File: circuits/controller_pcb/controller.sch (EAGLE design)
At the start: 26 parts, among them J1 USB-MICROB, Q1 BSS138, Q2 FDN340P, U1 ATMEGA328P_TQFP, Y2 12MHz

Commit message: Merged multiple board into a single one - controller - UNTESTED
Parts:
- removed J1: USB-MICROB, SparkFun-Connectors:USB-MICROB
- removed Q1: BSS138, SparkFun-DiscreteSemi:MOSFET-NCHANNELBSS138
- removed R1: 10k, rcl:R-EU_R0402
- removed Y2: 12MHz, crystals_golledge_full_v1-0:GSX-531
- added C11, C12, C13, C14, C15, C8: 100n, rcl:C-EUC0402K
- added IC1: DS1820, DS1820:DS1820
- added J3: USB-MICROB", SparkFun-Connectors:USB-MICROB"
- added Q3: SI2333DS, transistor-fet:SI2333DS
- added Q5: BSS138, transistor-fet:BSS138
- added R10, R11: (no value), rcl:R-EU_R0402
- added R4, R8: 10k, rcl:R-EU_R0402
- added R5: 1k, rcl:R-EU_R0402
- added R6, R7: 4k7, rcl:R-EU_R0402
- added R9: 0.1, rcl:R-EU_R2512
- added TP1, TP2, TP3, TP5, TP6, TP7: TPTP07SQ, testpad:TPTP07SQ
- added U$7: 1X6, headers(.05in):1X6
- added U$8: INA219AIDCNR, INA219AIDCNR:INA219AIDCNR
- added U$9: 12MHz, crystals_golledge_full_v1-0:GSX-331
- added U2: MIC5219 5V, SparkFun-PowerIC:V_REG_MIC52195V
- C1: value 22p -> 47u; device rcl:C-EUC0402K -> rcl:C-EUC1206
- C2: value 22p -> 10u; device rcl:C-EUC0402K -> rcl:C-EUC0603K
- C3: value 22p -> 100n
- C6, C7, C9: value 100n -> 22p
- R2, R3: value (none) -> 10k
- U$1: value 1X3 -> DRV8835DSSR; device headers(.05in):1X3 -> DRV8835:DRV8835DSSR
- U$2: value 1X3 -> CH340G; device headers(.05in):1X3 -> ch340g:CH340G
- U$3, U$4: value 1X8MALE -> 504050; device headers(.05in):1X8MALE -> con-molex-picolock:504050
- U$5: value CH340G -> MG996R_MOTOR; device ch340g:CH340G -> MG996R-Motor:MG996R_MOTOR
- U$6: value 16Mhz -> 16MHz
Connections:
- net N$13 renamed LED_R_
- net N$14 renamed LED_G_
- removed net CS: U1.PB2(SS/OC1B)
- removed net DATA_DIR_BIT: Q1.G, U1.PD2(INT0)
- removed net DI: U1.PD6(AIN0)
- removed net DIR: U1.PB0(ICP)
- removed net DS18B20: U1.PD5(T1)
- removed net EN: U1.PD7(AIN1)
- removed net N$15: LED1.B, RN1B.2
- removed net N$6: F1.1, J1.VBUS
- removed net N$7: Q1.S, U1.PD1(TXD)
- removed net PWM_1: U$2.3, U1.ADC7
- removed net SCK: U1.PB5(SCK)
- removed net SI: U1.PB3(MOSI/OC2)
- removed net SO: U1.PB4(MISO)
- new net 1WIRE: IC1.DQ, R7.2, U1.PD4(XCK/T0)
- new net IN1/PHASE: U$1.AIN1/APHASE, U$1.BIN1/BPHASE, U1.PB1(OC1A)
- new net IN2/ENBL: U$1.AIN2/AENBL, U$1.BIN2/BENBL, U1.PB2(SS/OC1B)
- new net LED_B: RN1A.1, U1.PC1(ADC1)
- new net LED_B_: LED1.B, RN1A.2
- new net LED_G: RN1C.1, U1.PC0(ADC0)
- new net LED_R: RN1D.1, U1.ADC7
- new net MODE: U$1.MODE, U1.PB0(ICP)
- new net MOT+: U$1.AOUT1, U$1.BOUT1, U$5.MOT-
- new net MOT-: U$1.AOUT2, U$1.BOUT2, U$5.MOT+
- new net N$12: C13.1, U2.BP
- new net N$14: TP1.TP, U1.PB5(SCK)
- new net VCC: Q3.D, R8.2, U$3.2, U$4.2
- new net VDD: C15.1, R9.1, U$1.VM, U$8.IN-
- new net VIN_ADC: R10.1, R11.2, U1.PC3(ADC3)
- net 5V: now also C14.1, C2.1, C4.1, IC1.VDD, R2.2, R3.2, R4.2, R6.1, R7.1, TP6.TP, U$1.VCC, U$7.3, U$8.VS, U2.OUT; no longer C7.1, C9.1, R1.2, U$2.1, U$5.VCC
- net D+: now also J3.D+, U$2.D+; no longer J1.D+, U$5.D+
- net D-: now also J3.D-, U$2.D-; no longer J1.D-, U$5.D-
- net DATA: now also Q5.D, R5.2, R6.2, U$3.3, U$4.3; no longer Q1.D, U1.PD0(RXD)
- net GND: now also C11.2, C12.2, C13.2, C14.2, C15.2, C8.2, IC1.GND, J3.GND, J3.SHIELD, Q3.G, Q5.S, R11.1, R8.1, TP7.TP, U$1.GND, U$1.PGND, U$2.GND, U$3.1, U$4.1, U$6.2, U$6.4, U$7.5, U$8.A0, U$8.A1, U$8.GND, U$9.2, U$9.4, U2.GND; no longer C3.2, J1.GND, R2.1, U$1.2, U$5.GND
- net INT: now also U$7.1, U1.PD2(INT0); no longer U$2.2, U1.ADC6
- net N$1: now also C6.1, U$6.1, U1.PB7(XTAL2/TOSC2); no longer C2.1, U$5.XO, Y2.1
- net N$10: now also C11.1, F1.1, J3.VBUS, U$2.VCC; no longer RN1C.1, U1.PC2(ADC2)
- net N$11: now also C8.1, U$2.V3; no longer RN1D.1, U1.PC1(ADC1)
- net N$2: now also C7.1, U$6.3, U1.PB6(XTAL1/TOSC1); no longer C3.1, U$5.XI, Y2.3
- net N$3: now also TP3.TP, U1.PB3(MOSI/OC2); no longer C1.1, U$6.3, U1.PB7(XTAL2/TOSC2)
- net N$4: now also TP2.TP, U1.PB4(MISO); no longer C4.1, U$5.V3
- net N$5: now also C3.1, U$2.DTR; no longer C10.1, U$6.1, U1.PB6(XTAL1/TOSC1)
- net N$8: now also C10.1, U$2.XI, U$9.3; no longer R2.2, R3.1, U1.PC0(ADC0)
- net N$9: now also C9.1, U$2.XO, U$9.1; no longer RN1B.1, U1.PC3(ADC3)
- net PWM: now also U$7.2, U1.PD3(INT1); no longer U1.PB1(OC1A)
- net RST: now also C3.2, R4.1, TP5.TP; no longer C6.1, R1.1
- net RX: now also R5.1, U$2.TX, U1.PD0(RXD); no longer U$5.RX, U1.PD3(INT1)
- net SCL: now also R3.1, U$7.6, U$8.SCL; no longer U$1.1
- net SDA: now also R2.1, U$7.4, U$8.SDA; no longer U$1.3
- net TX: now also Q5.G, U$2.RX, U1.PD1(TXD); no longer U$5.TX, U1.PD4(XCK/T0)
- net VIN: now also C1.1, C12.1, Q3.S, R10.2, R9.2, U$8.IN+, U2.EN, U2.IN; no longer R3.2
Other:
- note removed: "+5V selector (USB)"
- note removed: "ADD reset to breakout pins"
- moved on the sheet: C1, C10, C2, C3, C4, C5, C6, C7, C9, F1, LED1, Q2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

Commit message: Updated controller circuit - UNTESTED
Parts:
- removed U$7: 1X6, headers(.05in):1X6
- added D1: IN5819, SparkFun-DiscreteSemi:MBRA140
- added MISO, SCK: TPTP07SQ, testpad:TPTP07SQ
- added RN2: (no value), resistor-dil:4R-NYC124
- added U$10: 1X5, headers(.05in):1X5
- R5: value 1k -> 10k
- TP1, TP2: value TPTP07SQ -> PTR1TP12R; device testpad:TPTP07SQ -> testpad:PTR1TP12R
- renumbered TP3 to MOSI, TP5 to RST, TP6 to 5V, TP7 to GND
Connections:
- removed net PWM: U$7.2, U1.PD3(INT1)
- new net HD_DIR: Q5.G, R5.2, U1.PD3(INT1)
- new net N$13: TP2.TP, U1.PD5(T1)
- new net N$15: RN2A.2, U$2.RX
- new net N$6: RN2D.2, U$2.TX
- new net N$7: TP1.TP, U$3.4, U$4.4
- net 5V: now also U$10.2, U$2.VCC; no longer U$7.3
- net DATA: now also D1.A, Q5.S; no longer Q5.D, R5.2
- net GND: now also R5.1, U$10.4; no longer Q5.S, U$7.5
- net INT: now also U$10.1; no longer U$7.1
- net N$10: no longer U$2.VCC
- net N$14: now also SCK.TP; no longer TP1.TP
- net N$4: now also MISO.TP; no longer TP2.TP
- net RX: now also Q5.D, RN2D.1; no longer R5.1, U$2.TX
- net SCL: now also U$10.5; no longer U$7.6
- net SDA: now also U$10.3; no longer U$7.4
- net TX: now also D1.C, RN2A.1; no longer Q5.G, U$2.RX
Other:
- moved on the sheet: C10, C11, C14, C15, C3, C8, C9, F1, J3, Q2, Q5, R10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

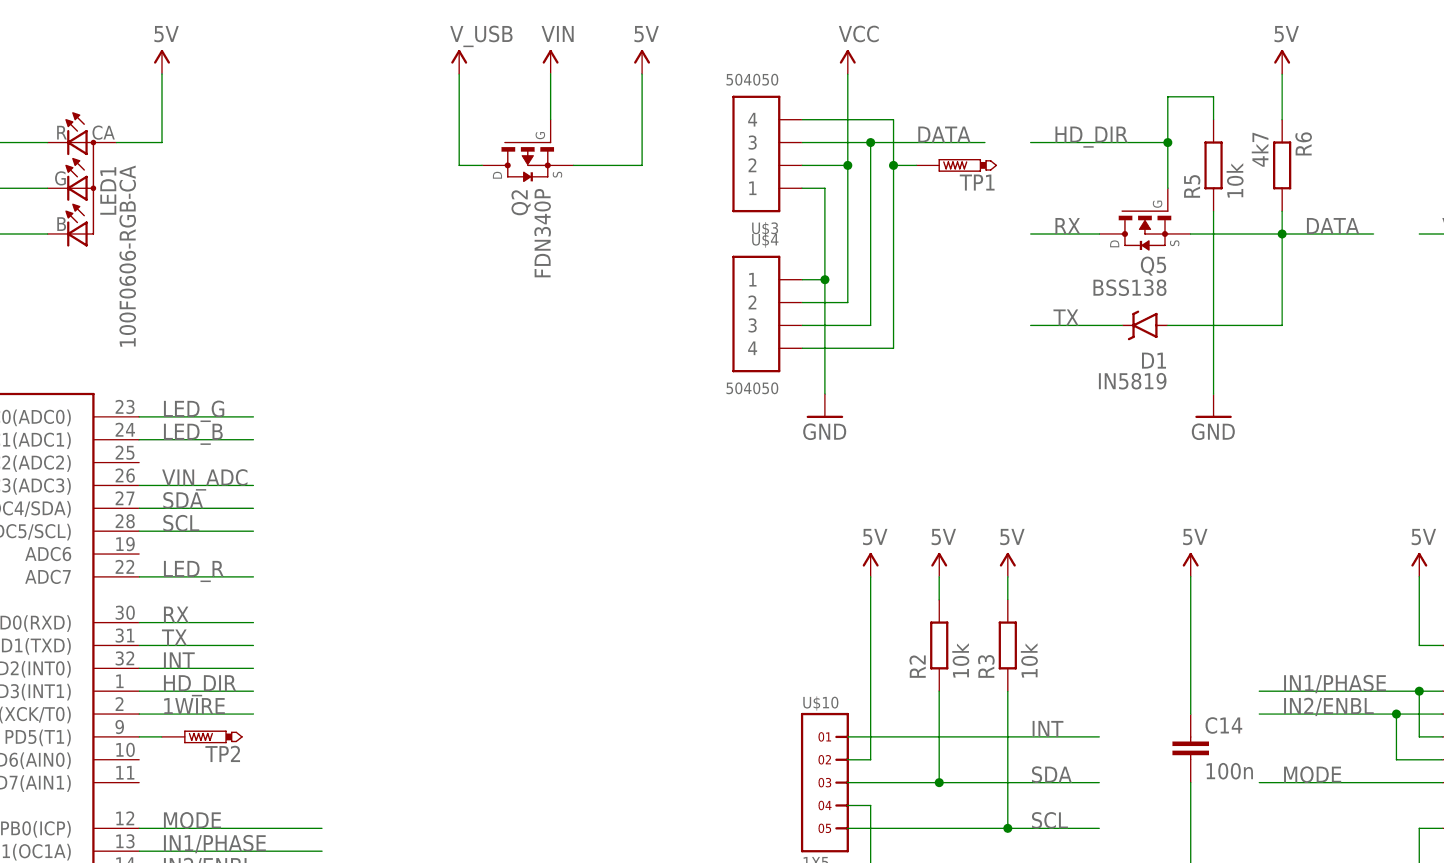
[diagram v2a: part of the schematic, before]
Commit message: Corrected Q5 orientation - UNTESTED
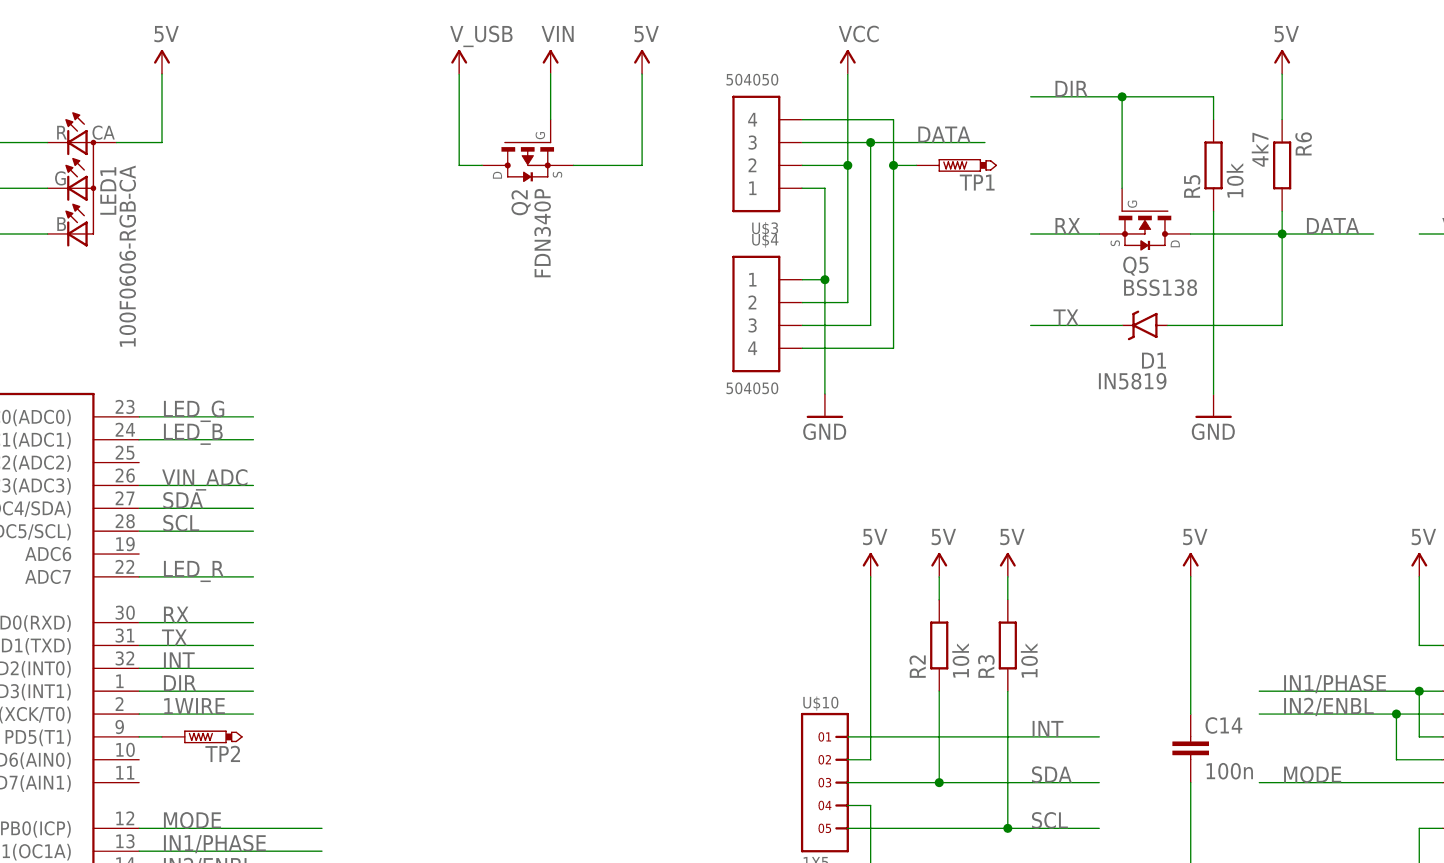
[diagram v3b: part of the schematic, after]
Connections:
- net HD_DIR renamed DIR
- net DATA: now also Q5.D; no longer Q5.S
- net RX: now also Q5.S; no longer Q5.D
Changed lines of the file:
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@@
 <grid distance="0.1" unitdist="inch" unit="inch" style="lines" multiple="1" display="no" altdistance="0.01" altunitdist="inch" altunit="inch"/>
 <layers>
-<layer number="1" name="Top" color="4" fill="1" visible="yes" active="no"/>
-<layer number="16" name="Bottom" color="1" fill="1" visible="yes" active="no"/>
-<layer number="17" name="Pads" color="2" fill="1" visible="yes" active="no"/>
-<layer number="18" name="Vias" color="2" fill="1" visible="yes" active="no"/>
-<layer number="19" name="Unrouted" color="6" fill="1" visible="yes" active="no"/>
-<layer number="20" name="Dimension" color="15" fill="1" visible="yes" active="no"/>
-<layer number="21" name="tPlace" color="7" fill="1" visible="yes" active="no"/>
-<layer number="22" name="bPlace" color="7" fill="1" visible="yes" active="no"/>
-<layer number="23" name="tOrigins" color="15" fill="1" visible="yes" active="no"/>
-<layer number="24" name="bOrigins" color="15" fill="1" visible="yes" active="no"/>
-<layer number="25" name="tNames" color="7" fill="1" visible="yes" active="no"/>
-<layer number="26" name="bNames" color="7" fill="1" visible="yes" active="no"/>
-<layer number="27" name="tValues" color="7" fill="1" visible="yes" active="no"/>
-<layer number="28" name="bValues" color="7" fill="1" visible="yes" active="no"/>
+<layer number="1" name="Top" color="4" fill="1" visible="no" active="no"/>
+<layer number="16" name="Bottom" color="1" fill="1" visible="no" active="no"/>
+<layer number="17" name="Pads" color="2" fill="1" visible="no" active="no"/>
+<layer number="18" name="Vias" color="2" fill="1" visible="no" active="no"/>
+<layer number="19" name="Unrouted" color="6" fill="1" visible="no" active="no"/>
+<layer number="20" name="Dimension" color="15" fill="1" visible="no" active="no"/>
+<layer number="21" name="tPlace" color="7" fill="1" visible="no" active="no"/>
+<layer number="22" name="bPlace" color="7" fill="1" visible="no" active="no"/>
+<layer number="23" name="tOrigins" color="15" fill="1" visible="no" active="no"/>
+<layer number="24" name="bOrigins" color="15" fill="1" visible="no" active="no"/>
+<layer number="25" name="tNames" color="7" fill="1" visible="no" active="no"/>
+<layer number="26" name="bNames" color="7" fill="1" visible="no" active="no"/>
+<layer number="27" name="tValues" color="7" fill="1" visible="no" active="no"/>
+<layer number="28" name="bValues" color="7" fill="1" visible="no" active="no"/>
 <layer number="29" name="tStop" color="7" fill="3" visible="no" active="no"/>
 <layer number="30" name="bStop" color="7" fill="6" visible="no" active="no"/>
@@
 <layer number="35" name="tGlue" color="7" fill="4" visible="no" active="no"/>
 <layer number="36" name="bGlue" color="7" fill="5" visible="no" active="no"/>
-<layer number="37" name="tTest" color="7" fill="1" visible="yes" active="no"/>
-<layer number="38" name="bTest" color="7" fill="1" visible="yes" active="no"/>
+<layer number="37" name="tTest" color="7" fill="1" visible="no" active="no"/>
+<layer number="38" name="bTest" color="7" fill="1" visible="no" active="no"/>
 <layer number="39" name="tKeepout" color="4" fill="11" visible="no" active="no"/>
 <layer number="40" name="bKeepout" color="1" fill="11" visible="no" active="no"/>
@@
 <layer number="44" name="Drills" color="7" fill="1" visible="no" active="no"/>
 <layer number="45" name="Holes" color="7" fill="1" visible="no" active="no"/>
-<layer number="46" name="Milling" color="3" fill="1" visible="yes" active="no"/>
-<layer number="47" name="Measures" color="7" fill="1" visible="yes" active="no"/>
-<layer number="48" name="Document" color="7" fill="1" visible="yes" active="no"/>
-<layer number="49" name="Reference" color="7" fill="1" visible="yes" active="no"/>
-<layer number="50" name="dxf" color="7" fill="1" visible="yes" active="no"/>
-<layer number="51" name="tDocu" color="7" fill="1" visible="yes" active="no"/>
-<layer number="52" name="bDocu" color="7" fill="1" visible="yes" active="no"/>
-<layer number="53" name="tGND_GNDA" color="7" fill="9" visible="yes" active="no"/>
-<layer number="54" name="bGND_GNDA" color="1" fill="9" visible="yes" active="no"/>
-<layer number="56" name="wert" color="7" fill="1" visible="yes" active="no"/>
-<layer number="57" name="tCAD" color="7" fill="1" visible="yes" active="no"/>
-<layer number="59" name="tCarbon" color="7" fill="1" visible="yes" active="no"/>
-<layer number="60" name="bCarbon" color="7" fill="1" visible="yes" active="no"/>
+<layer number="46" name="Milling" color="3" fill="1" visible="no" active="no"/>
+<layer number="47" name="Measures" color="7" fill="1" visible="no" active="no"/>
+<layer number="48" name="Document" color="7" fill="1" visible="no" active="no"/>
+<layer number="49" name="Reference" color="7" fill="1" visible="no" active="no"/>
+<layer number="50" name="dxf" color="7" fill="1" visible="no" active="no"/>
+<layer number="51" name="tDocu" color="7" fill="1" visible="no" active="no"/>
+<layer number="52" name="bDocu" color="7" fill="1" visible="no" active="no"/>
+<layer number="53" name="tGND_GNDA" color="7" fill="9" visible="no" active="no"/>
+<layer number="54" name="bGND_GNDA" color="1" fill="9" visible="no" active="no"/>
+<layer number="56" name="wert" color="7" fill="1" visible="no" active="no"/>
+<layer number="57" name="tCAD" color="7" fill="1" visible="no" active="no"/>
+<layer number="59" name="tCarbon" color="7" fill="1" visible="no" active="no"/>
+<layer number="60" name="bCarbon" color="7" fill="1" visible="no" active="no"/>
 <layer number="90" name="Modules" color="5" fill="1" visible="yes" active="yes"/>
 <layer number="91" name="Nets" color="2" fill="1" visible="yes" active="yes"/>
@@
 <instance part="SUPPLY26" gate="G$1" x="213.36" y="91.44"/>
 <instance part="GND24" gate="1" x="213.36" y="53.34"/>
-<instance part="Q5" gate="G$1" x="208.28" y="129.54" smashed="yes" rot="MR270">
-<attribute name="VALUE" x="210.82" y="124.46" size="1.778" layer="96" rot="R180"/>
-<attribute name="NAME" x="210.82" y="127" size="1.778" layer="95" rot="R180"/>
+<instance part="Q5" gate="G$1" x="208.28" y="129.54" smashed="yes" rot="R270">
+<attribute name="VALUE" x="205.74" y="124.46" size="1.778" layer="96" rot="MR180"/>
+<attribute name="NAME" x="205.74" y="127" size="1.778" layer="95" rot="MR180"/>
 </instance>
 <instance part="R10" gate="G$1" x="254" y="137.16" rot="R90"/>
@@
 <wire x1="195.58" y1="129.54" x2="203.2" y2="129.54" width="0.1524" layer="91"/>
 <label x="198.12" y="129.54" size="1.778" layer="95"/>
-<pinref part="Q5" gate="G$1" pin="D"/>
+<pinref part="Q5" gate="G$1" pin="S"/>
 </segment>
 <segment>
@@
 <wire x1="223.52" y1="119.38" x2="223.52" y2="129.54" width="0.1524" layer="91"/>
 <junction x="223.52" y="129.54"/>
-<pinref part="Q5" gate="G$1" pin="S"/>
-<wire x1="223.52" y1="129.54" x2="213.36" y2="129.54" width="0.1524" layer="91"/>
+<pinref part="Q5" gate="G$1" pin="D"/>
+<wire x1="213.36" y1="129.54" x2="223.52" y2="129.54" width="0.1524" layer="91"/>
 </segment>
 <segment>
@@
 </segment>
 </net>
-<net name="HD_DIR" class="0">
-<segment>
+<net name="DIR" class="0">
+<segment>
+<pinref part="R5" gate="G$1" pin="2"/>
+<wire x1="215.9" y1="142.24" x2="215.9" y2="144.78" width="0.1524" layer="91"/>
+<wire x1="215.9" y1="144.78" x2="205.74" y2="144.78" width="0.1524" layer="91"/>
+<label x="198.12" y="144.78" size="1.778" layer="95"/>
+<wire x1="205.74" y1="144.78" x2="195.58" y2="144.78" width="0.1524" layer="91"/>
 <pinref part="Q5" gate="G$1" pin="G"/>
-<wire x1="210.82" y1="134.62" x2="210.82" y2="139.7" width="0.1524" layer="91"/>
-<pinref part="R5" gate="G$1" pin="2"/>
-<wire x1="210.82" y1="139.7" x2="210.82" y2="144.78" width="0.1524" layer="91"/>
-<wire x1="215.9" y1="142.24" x2="215.9" y2="144.78" width="0.1524" layer="91"/>
-<wire x1="215.9" y1="144.78" x2="210.82" y2="144.78" width="0.1524" layer="91"/>
-<label x="198.12" y="139.7" size="1.778" layer="95"/>
-<wire x1="210.82" y1="139.7" x2="195.58" y2="139.7" width="0.1524" layer="91"/>
-<junction x="210.82" y="139.7"/>
-</segment>
-<segment>
+<wire x1="205.74" y1="134.62" x2="205.74" y2="144.78" width="0.1524" layer="91"/>
+<junction x="205.74" y="144.78"/>
+</segment>
+<segment>
